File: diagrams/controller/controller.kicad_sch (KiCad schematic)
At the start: 4 parts, among them SW1 SW_Push, U1 ESP32-WROOM-32

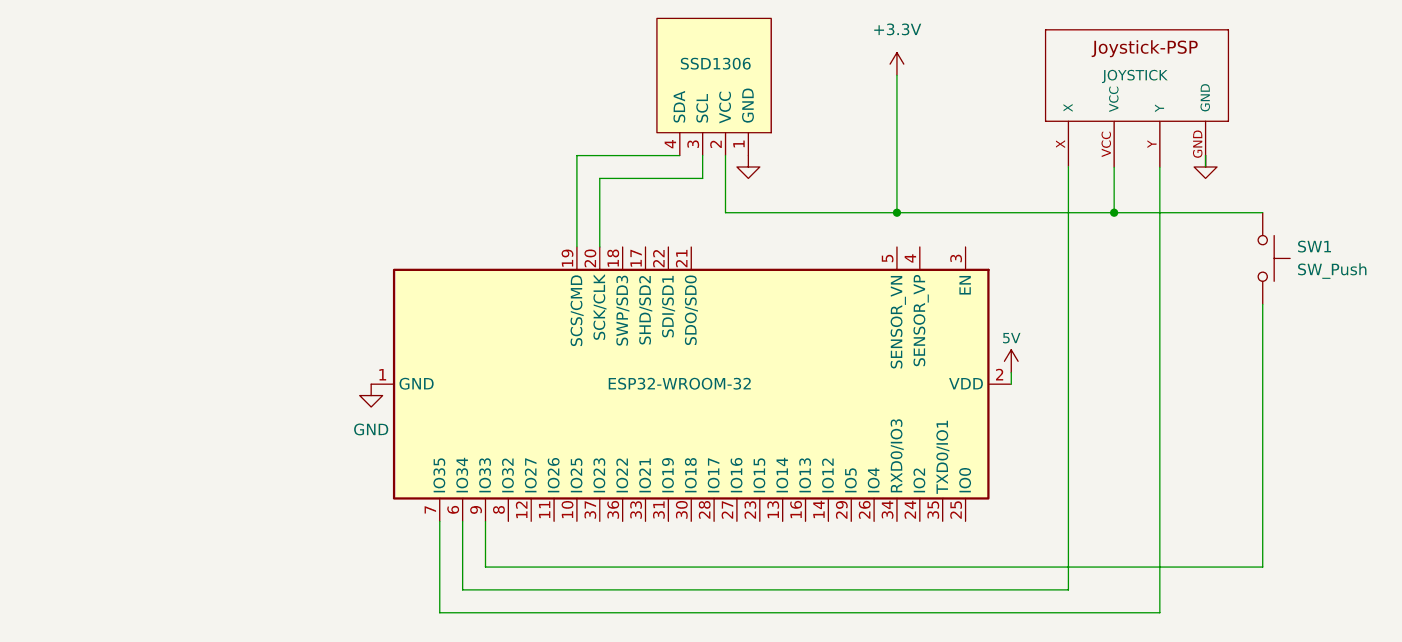
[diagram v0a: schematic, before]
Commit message: "Added sleep and battery management functionality"
Updated several files to include power management functionalities as well as adjustments necessary for proper communication between the controller and car modules.

In "config.h" file, introduced new variables for battery pin, and changed the broadcast address for communication. Adjusted timer configurations for proper sleep intervals.

In "State.h" and "State.cpp" files, introduced validity checks and sleep flags to manage controller behavior. Replaced the Timer0_ISR method to handle a goToSleep flag which can be used to place the device into deep sleep mode.

In the "main.cpp" files in both car and controller module, incorporated new logic for initializing and adjusting for battery reading, while also including clean up and sleeping when needed.

Also updated robot diagrams to reflect changes in circuitry and information transmission.

These changes are crucial for correct controller behavior and power conservation. Also optimized movement commands for smoother vehicle operation.
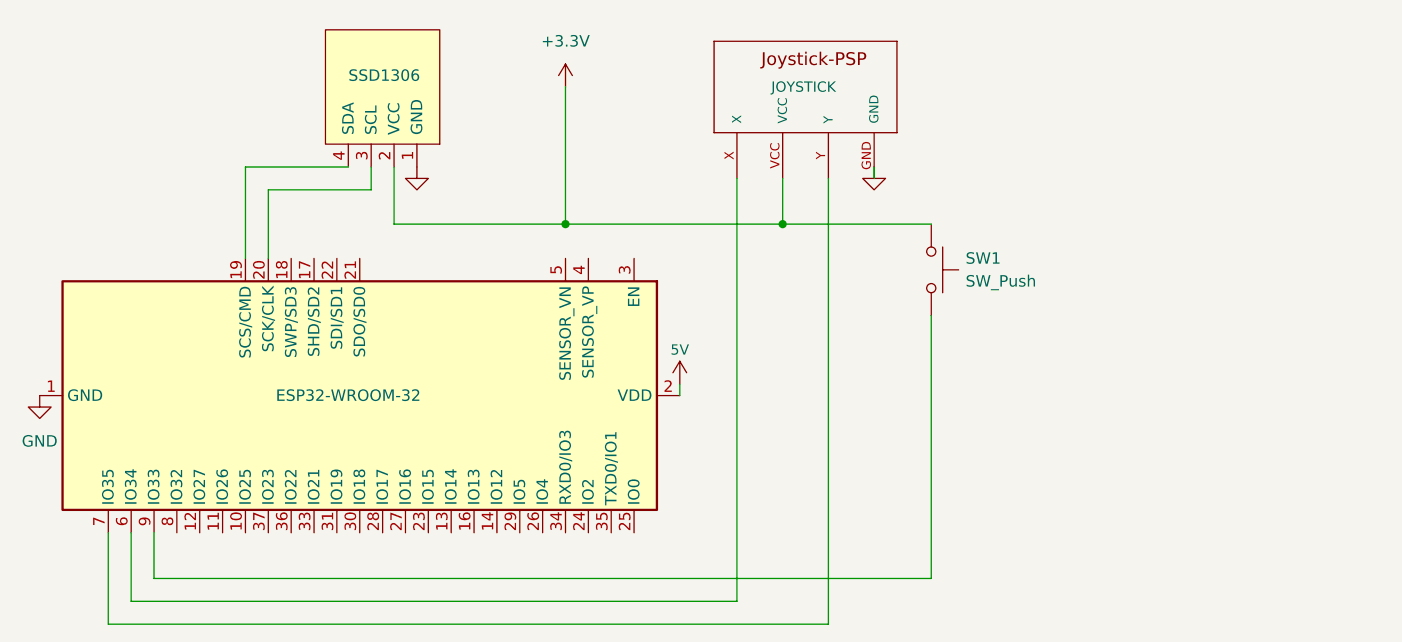
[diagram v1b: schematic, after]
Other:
- moved on the sheet: SW1
